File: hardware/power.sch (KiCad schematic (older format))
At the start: 10 parts, among them U4 TPS62736

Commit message: Update the part number for R13
The part number was specified as `603-RC0603FR-071KL` but should have
been `RC0603FR-07715KL`. The part number in the schematic has been
updated to reflect this.
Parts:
- R13: Part Number RC0603FR-071KL -> RC0603FR-07715KL
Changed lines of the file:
@@
 F 2 "Resistor_SMD:R_0603_1608Metric" V 7265 4115 50  0001 C CNN
 F 3 "~" H 7225 4125 50  0001 C CNN
-F 4 "RC0603FR-071KL" H 7225 4125 50  0001 C CNN "Part Number"
+F 4 "RC0603FR-07715KL" H 7225 4125 50  0001 C CNN "Part Number"
 	1    7225 4125
 	1    0    0    -1

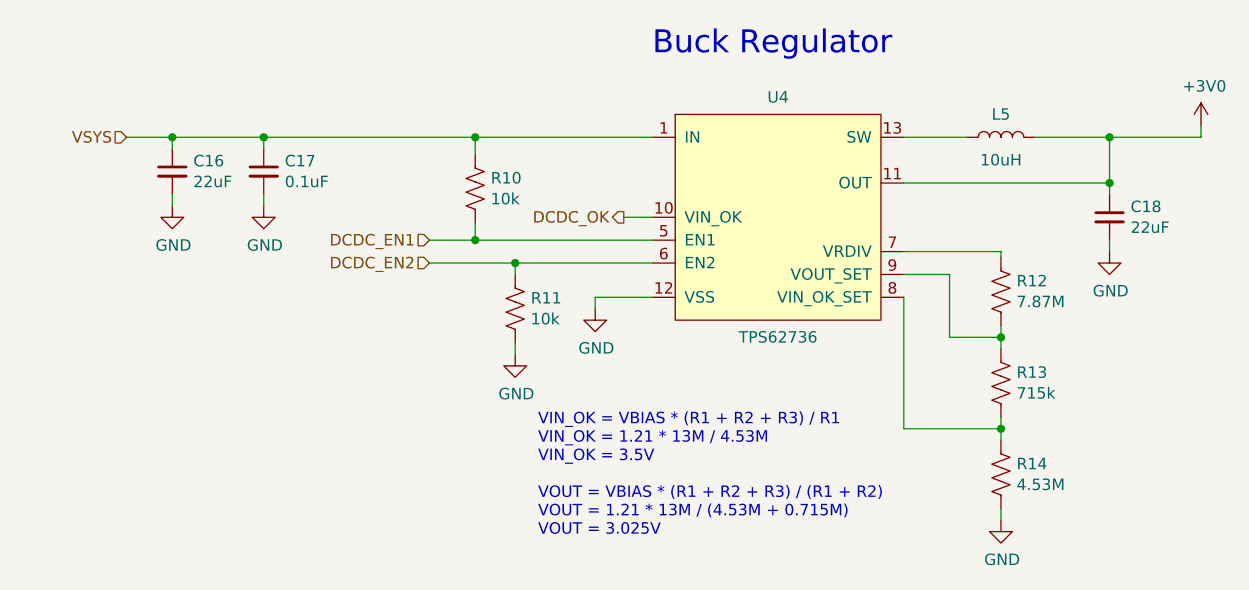
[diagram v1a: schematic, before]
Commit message: Invert pull-up/down supply for R10, R11
The voltage for these resistors was wrong, so the 3V buck was configured
to be in ship mode by default.

The 3V buck will now start in enable mode with the following
configuration:

- R10 (EN2) = 1
- R11 (EN1) = 0
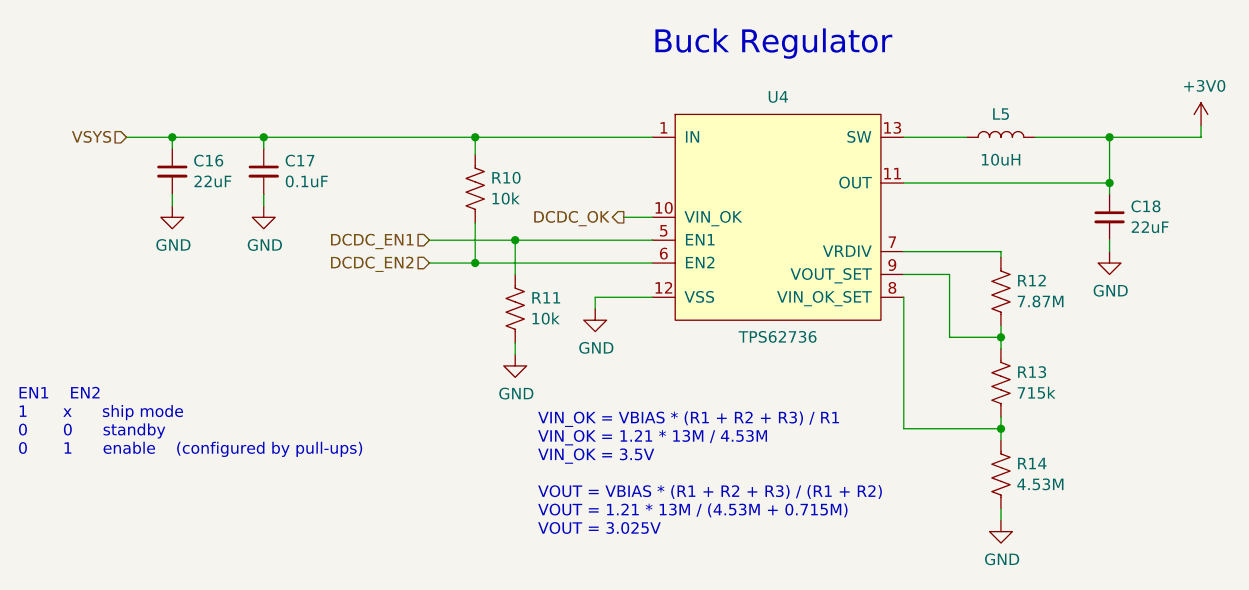
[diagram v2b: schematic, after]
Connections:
- net DCDC_EN1: now also R11.1; no longer R10.2
- net DCDC_EN2: now also R10.2; no longer R11.1
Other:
- note added: "EN1 EN2\n1 x ship mode\n0 0 standby\n0 1 enable (configured by pull-ups)"
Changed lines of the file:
@@
 	4925 3050 5700 3050
-Wire Wire Line
-	4925 3500 4925 3425
-Wire Wire Line
-	4925 3500 5700 3500
 Wire Wire Line
 	5575 3400 5700 3400
@@
 VIN_OK = VBIAS * (R1 + R2 + R3) / R1\nVIN_OK = 1.21 * 13M / 4.53M\nVIN_OK = 3.5V\n\nVOUT = VBIAS * (R1 + R2 + R3) / (R1 + R2)\nVOUT = 1.21 * 13M / (4.53M + 0.715M)\nVOUT = 3.025V
 Wire Wire Line
-	5100 3600 5700 3600
-Wire Wire Line
 	5100 4000 5100 3950
 $Comp
@@
 	1    0    0    -1
 $EndComp
-Wire Wire Line
-	5100 3650 5100 3600
 $Comp
 L Device:R_US R?
@@
 	1    0    0    -1
 $EndComp
-Connection ~ 5100 3600
 Wire Wire Line
-	4725 3600 5100 3600
-Connection ~ 4925 3500
-Wire Wire Line
-	4725 3500 4925 3500
+	4725 3600 4925 3600
 $Comp
 L power:+3V0 #PWR?
@@
 Text HLabel 4725 3600 0    50   Input ~ 0
 DCDC_EN2
+Wire Wire Line
+	4725 3500 5100 3500
+Wire Wire Line
+	4925 3600 4925 3425
+Connection ~ 4925 3600
+Wire Wire Line
+	4925 3600 5700 3600
+Wire Wire Line
+	5100 3650 5100 3500
+Connection ~ 5100 3500
+Wire Wire Line
+	5100 3500 5700 3500
+Text Notes 2925 4450 0    50   ~ 0
+EN1    EN2\n1       x      ship mode\n0       0      standby\n0       1      enable    (configured by pull-ups)
 $EndSCHEMATC
